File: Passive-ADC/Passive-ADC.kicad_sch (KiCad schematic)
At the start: 11 parts, among them J1 FPGA Terminal, J2 ADC Terminal

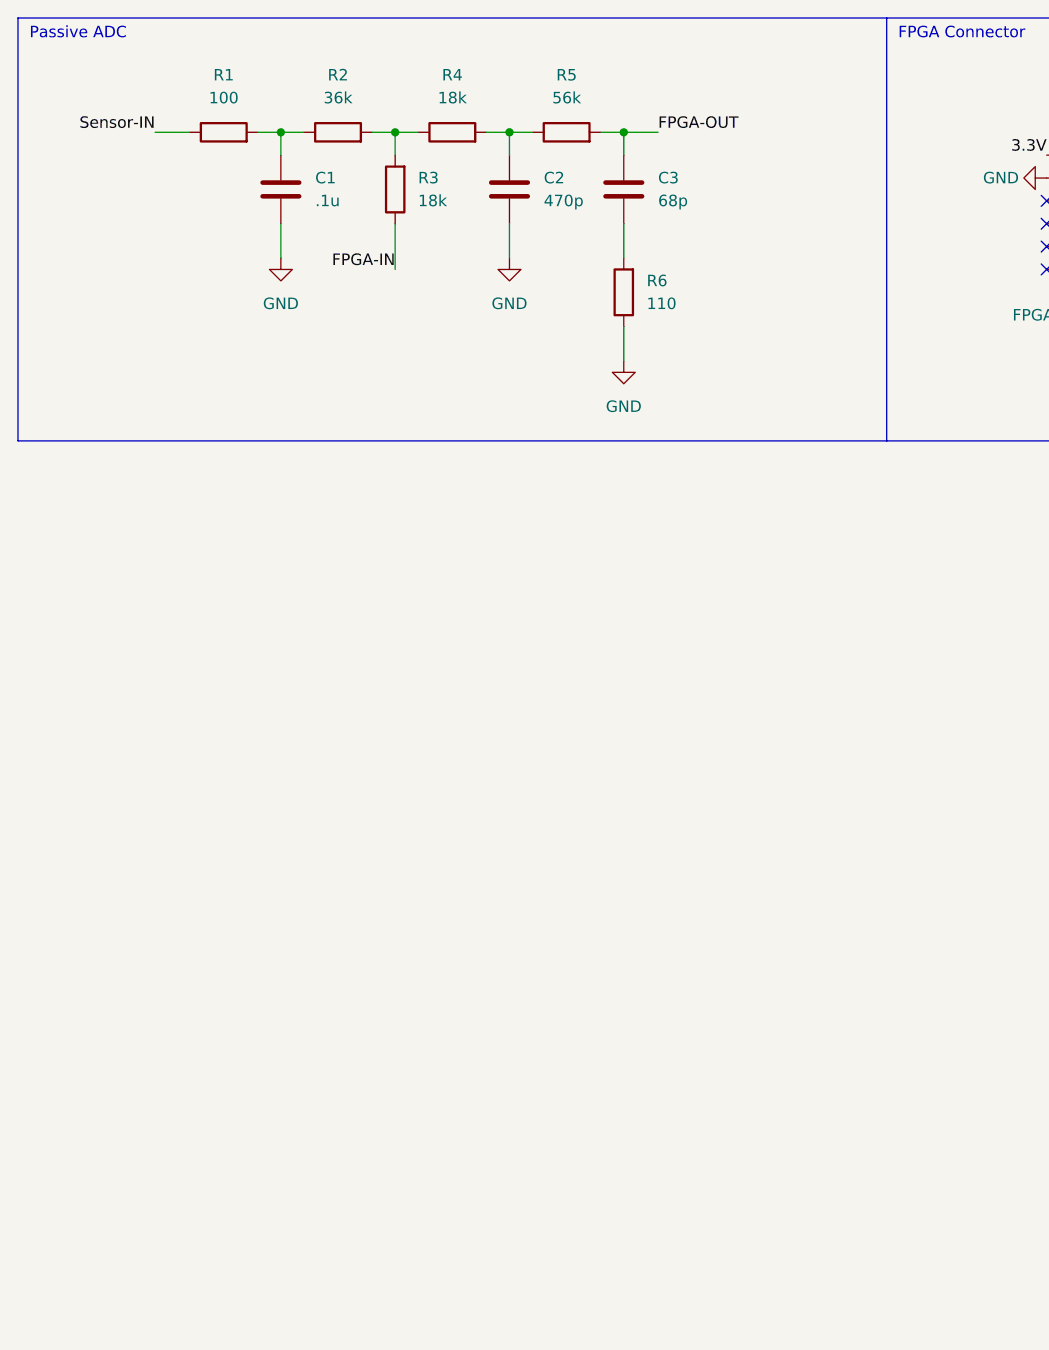
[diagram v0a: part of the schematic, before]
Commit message: Replaced passive adc with active adc
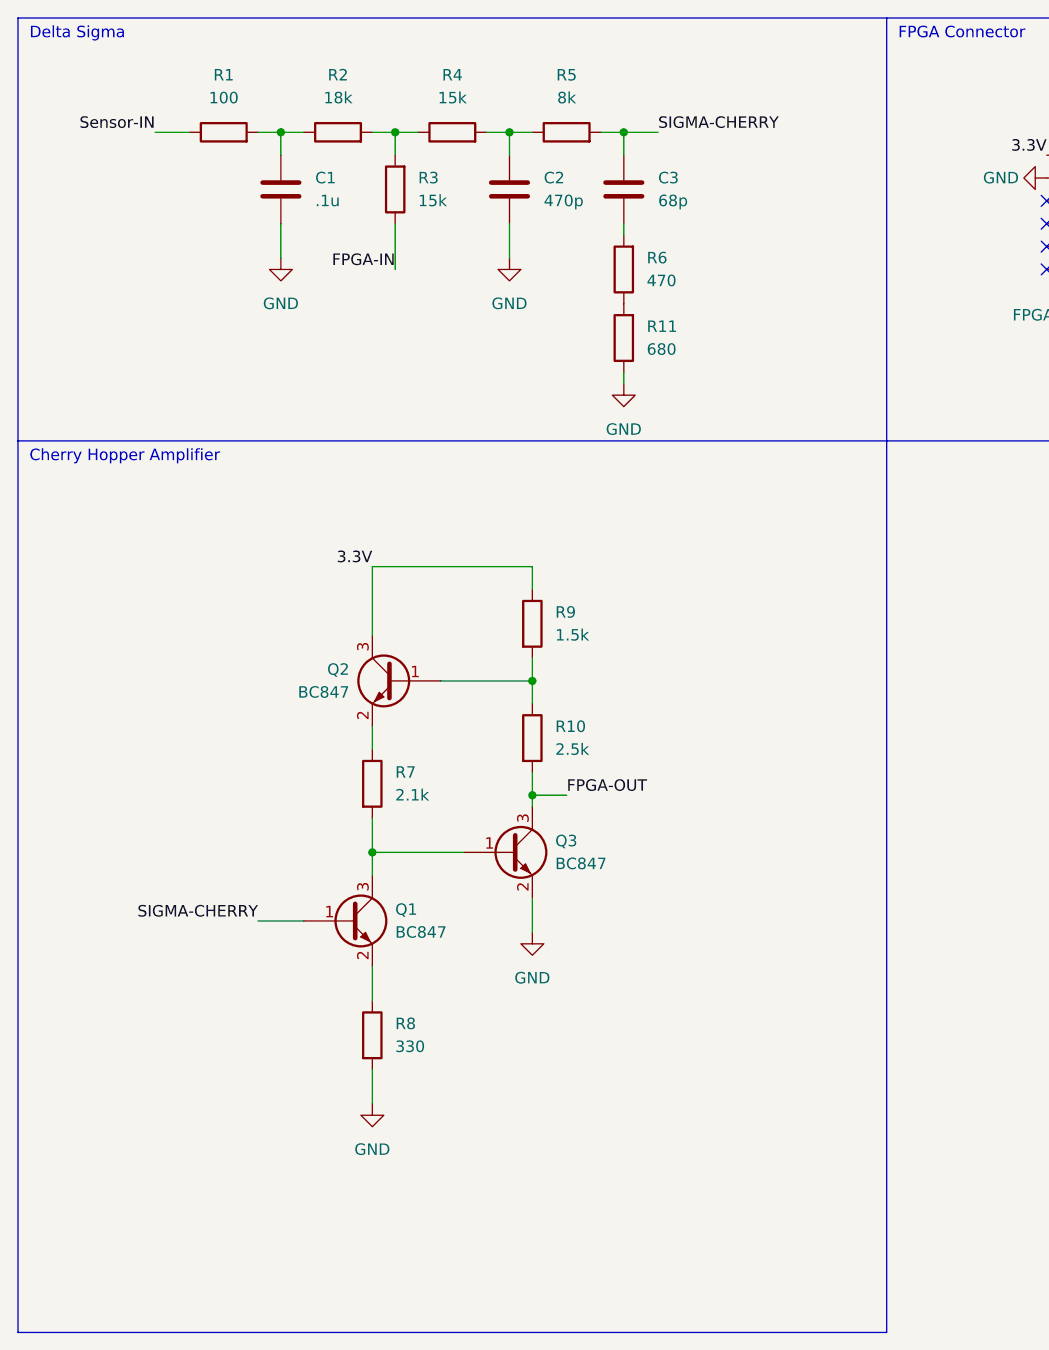
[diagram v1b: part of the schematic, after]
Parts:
- added Q1, Q2, Q3: BC847, Package_TO_SOT_SMD:SOT-23, symbol Transistor_BJT:BC847
- added R10: 2.5k, Resistor_SMD:R_0805_2012Metric_Pad1.20x1.40mm_HandSolder, symbol Device:R
- added R11: 680, Resistor_SMD:R_0805_2012Metric_Pad1.20x1.40mm_HandSolder, symbol Device:R
- added R7: 2.1k, Resistor_SMD:R_0805_2012Metric_Pad1.20x1.40mm_HandSolder, symbol Device:R
- added R8: 330, Resistor_SMD:R_0805_2012Metric_Pad1.20x1.40mm_HandSolder, symbol Device:R
- added R9: 1.5k, Resistor_SMD:R_0805_2012Metric_Pad1.20x1.40mm_HandSolder, symbol Device:R
- C1, C2, C3: footprint Capacitor_THT:CP_Radial_D7.5mm_P2.50mm -> Capacitor_SMD:C_0805_2012Metric_Pad1.18x1.45mm_HandSolder
- R1: footprint Resistor_THT:R_Axial_DIN0207_L6.3mm_D2.5mm_P10.16mm_Horizontal -> Resistor_SMD:R_0805_2012Metric_Pad1.20x1.40mm_HandSolder
- R2: value 36k -> 18k; footprint Resistor_THT:R_Axial_DIN0207_L6.3mm_D2.5mm_P10.16mm_Horizontal -> Resistor_SMD:R_0805_2012Metric_Pad1.20x1.40mm_HandSolder
- R3, R4: value 18k -> 15k; footprint Resistor_THT:R_Axial_DIN0207_L6.3mm_D2.5mm_P10.16mm_Horizontal -> Resistor_SMD:R_0805_2012Metric_Pad1.20x1.40mm_HandSolder
- R5: value 56k -> 8k; footprint Resistor_THT:R_Axial_DIN0207_L6.3mm_D2.5mm_P10.16mm_Horizontal -> Resistor_SMD:R_0805_2012Metric_Pad1.20x1.40mm_HandSolder
- R6: value 110 -> 470; footprint Resistor_THT:R_Axial_DIN0207_L6.3mm_D2.5mm_P10.16mm_Horizontal -> Resistor_SMD:R_0805_2012Metric_Pad1.20x1.40mm_HandSolder
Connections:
- net 3.3V: now also Q2.3 (C), R9.1
- net FPGA-OUT: now also Q3.3 (C), R10.2; no longer C3.1, R5.2
- net GND: now also Q3.2 (E), R11.1, R8.2; no longer R6.1
- new net: Q2.1 (B), R10.1, R9.2
- new net: Q2.2 (E), R7.1
- new net: R11.2, R6.1
- new net: Q1.2 (E), R8.1
- new net: Q1.3 (C), Q3.1 (B), R7.2
- new net SIGMA-CHERRY: C3.1, Q1.1 (B), R5.2
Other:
- note added: "Cherry Hopper Amplifier"
- note added: "Delta Sigma"
- note removed: "Passive ADC"
- moved on the sheet: R6

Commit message: Update passive curcuit with new resistor values
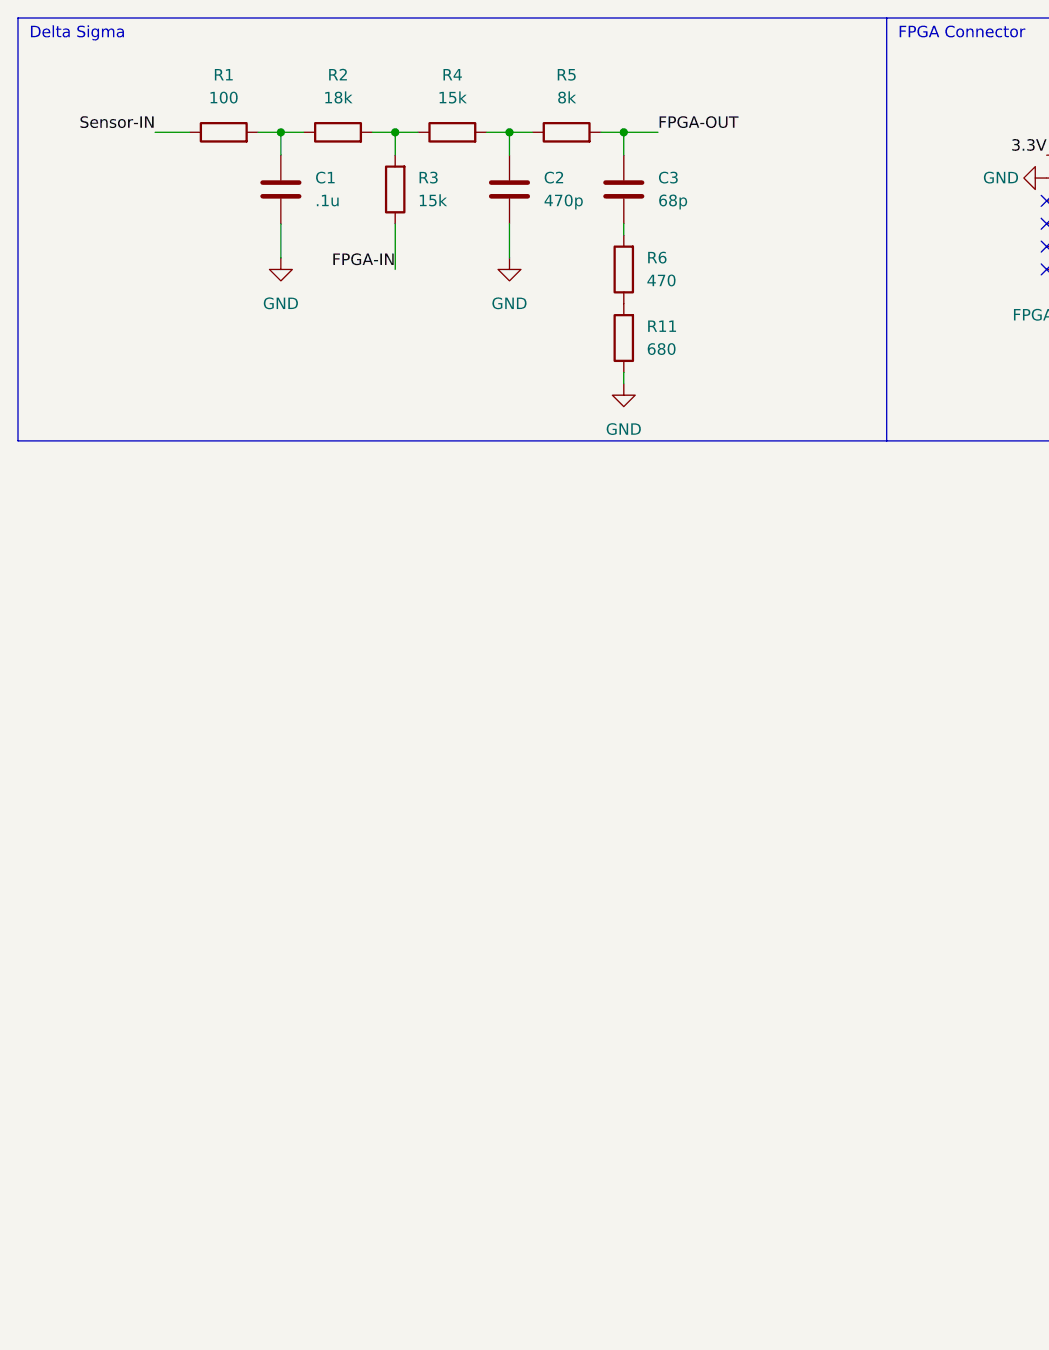
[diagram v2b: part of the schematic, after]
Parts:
- removed Q1, Q2, Q3: BC847, Package_TO_SOT_SMD:SOT-23, symbol Transistor_BJT:BC847
- removed R10: 2.5k, Resistor_SMD:R_0805_2012Metric_Pad1.20x1.40mm_HandSolder, symbol Device:R
- removed R7: 2.1k, Resistor_SMD:R_0805_2012Metric_Pad1.20x1.40mm_HandSolder, symbol Device:R
- removed R8: 330, Resistor_SMD:R_0805_2012Metric_Pad1.20x1.40mm_HandSolder, symbol Device:R
- removed R9: 1.5k, Resistor_SMD:R_0805_2012Metric_Pad1.20x1.40mm_HandSolder, symbol Device:R
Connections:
- net SIGMA-CHERRY is gone; now on net FPGA-OUT: C3.1, R5.2
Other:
- note removed: "Cherry Hopper Amplifier"
